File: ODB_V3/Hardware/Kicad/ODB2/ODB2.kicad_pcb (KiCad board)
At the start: 6 copper layers, 63.1 x 114.6 mm, 237 parts, among them IC1 W25Q512JVEIQ, J1 Screw_Terminal_01x08, J10 GPS_Conn_02x04_Top_Bottom, J11 Conn_02x04_Odd_Even, J15 Vin_XT30PW-F, J2 RFD_GT17HN-4DP-2HA56, J3 SYS_SW_Conn_01x05_Header, J5 MEM2067, J6 IdeFIX_GT17HN-4DP-2HA56, U1 STM32F412ZGTx, U10 ADXL382-2BCCZ-RL7, U11 SI5442DU-T1-GE3, U12 SI5442DU-T1-GE3, U13 L6981N33DR, U2 LM339, U3 SI5442DU-T1-GE3, U4 MS580301BA01-00, U6 BNO055, U7 MPQ9843GLE-5-AEC1-Z, U8 SI5442DU-T1-GE3, U9 MAX6612MXK, Y1 ABM8G-25.000MHZ-18-D2Y-T

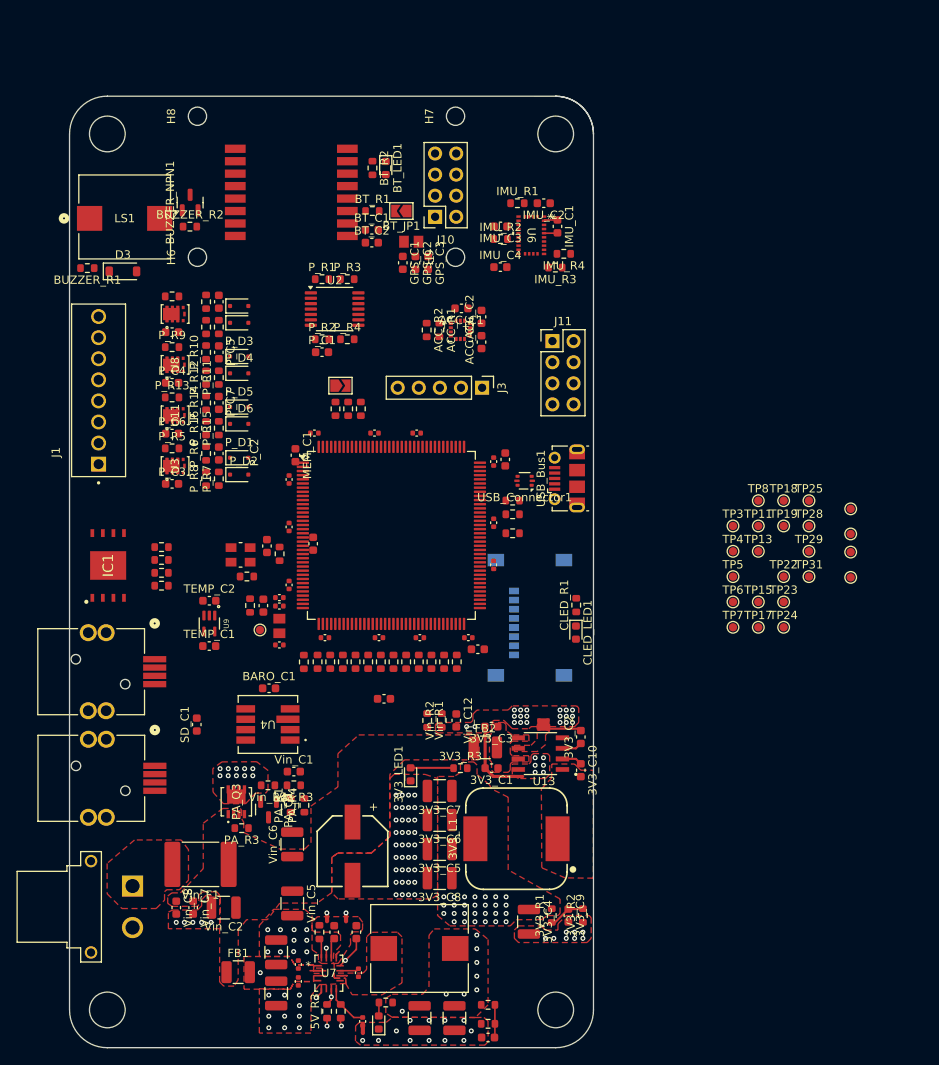
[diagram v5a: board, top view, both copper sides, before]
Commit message: fix: disconnected edge
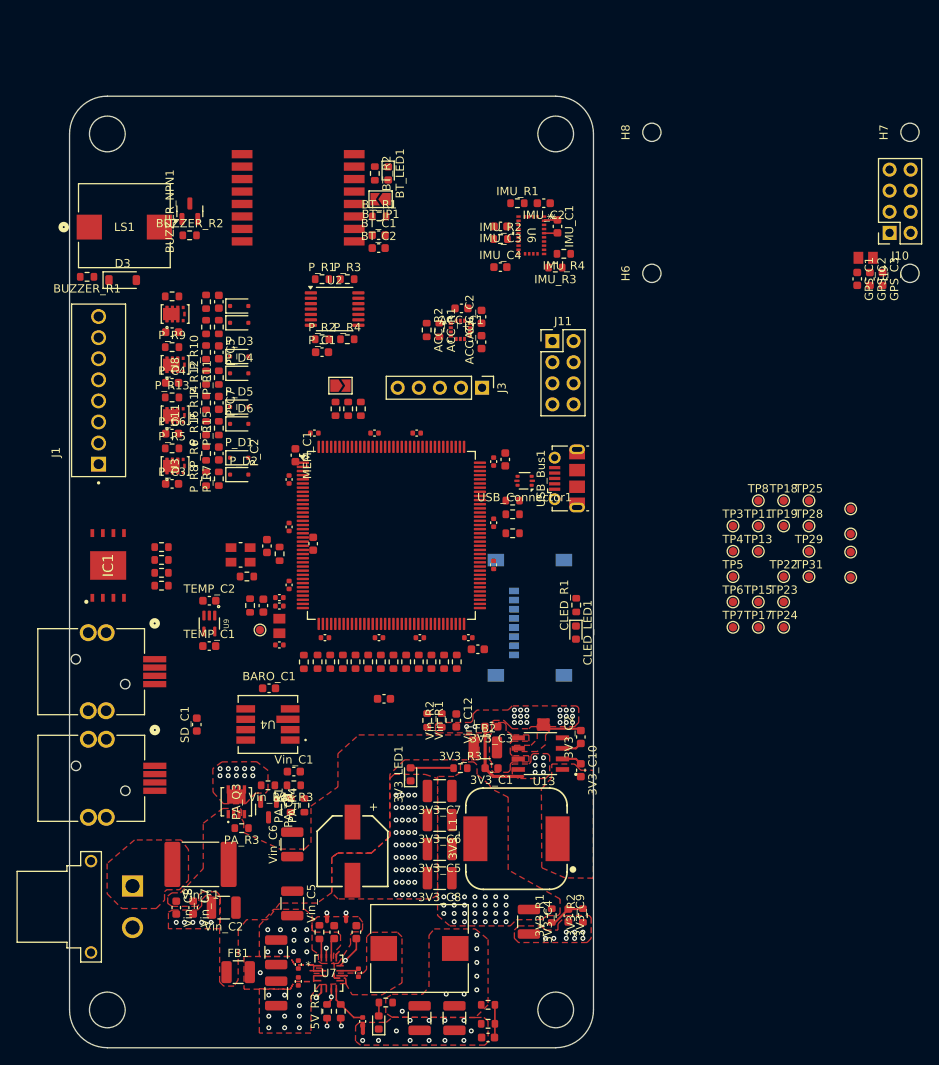
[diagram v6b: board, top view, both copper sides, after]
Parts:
- moved GPS_C1 54.8 mm to (212.3, 63.5)
- moved GPS_FB1 54.8 mm to (213.3, 60.9)
- moved J10 54.8 mm to (216.2, 57.9)
- moved GPS_C2 54.8 mm to (213.8, 63.5)
- moved GPS_C3 54.8 mm to (215.4, 63.5)
- moved H6 54.8 mm to (187.6, 62.8)
- moved H7 54.8 mm to (218.7, 45.8)
- moved H8 54.8 mm to (187.6, 45.8)
- moved H9 54.8 mm to (218.7, 62.8)
- moved BT_JP1 2.87 mm to (154.9, 53.9)
- moved BUZZER_R2 1.05 mm to (131.9, 58.2)
- moved BUZZER_NPN1 1.05 mm to (131.9, 55.3)
- moved BUZZER_R1 1.05 mm to (119.6, 63.2)
- moved D3 1.05 mm to (123.8, 63.6)
- moved LS1 1.05 mm to (124.1, 57.0)
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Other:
- outline, holes or cut-outs redrawn
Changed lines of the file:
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@@
 	(footprint "MountingHole:MountingHole_2.2mm_M2"
 		(layer "F.Cu")
-		(at 132.853519 43.866974 90)
+		(at 187.5846 45.8018 90)
 		(descr "Mounting Hole 2.2mm, M2, no annular, generated by kicad-footprint-generator mountinghole.py")
 		(tags "mountinghole M2")
@@
 	(footprint "ODB:SMTB-0927-TW-R_PUI"
 		(layer "F.Cu")
-		(at 124.087349 55.998685)
+		(at 124.0536 57.0484)
 		(tags "SMTB-0927-TW-R ")
 		(property "Reference" "LS1"
@@
 	(footprint "Capacitor_SMD:C_0603_1608Metric"
 		(layer "F.Cu")
-		(at 160.632273 61.534809 -90)
+		(at 215.363354 63.469635 -90)
 		(descr "Capacitor SMD 0603 (1608 Metric), square (rectangular) end terminal, IPC-7351 nominal, (Body size source: IPC-SM-782 page 76, https://www.pcb-3d.com/wordpress/wp-content/uploads/ipc-sm-782a_amendment_1_and_2.pdf), generated with kicad-footprint-generator")
 		(tags "capacitor")
@@
 	(footprint "MountingHole:MountingHole_2.2mm_M2"
 		(layer "F.Cu")
-		(at 163.937519 43.866974 90)
+		(at 218.6686 45.8018 90)
 		(descr "Mounting Hole 2.2mm, M2, no annular, generated by kicad-footprint-generator mountinghole.py")
 		(tags "mountinghole M2")
@@
 	(footprint "MountingHole:MountingHole_2.2mm_M2"
 		(layer "F.Cu")
-		(at 132.853519 60.853974 90)
+		(at 187.5846 62.7888 90)
 		(descr "Mounting Hole 2.2mm, M2, no annular, generated by kicad-footprint-generator mountinghole.py")
 		(tags "mountinghole M2")
@@
 	(footprint "Resistor_SMD:R_0603_1608Metric"
 		(layer "F.Cu")
-		(at 153.92012 55.285515)
+		(at 154.7436 55.9364)
 		(descr "Resistor SMD 0603 (1608 Metric), square (rectangular) end terminal, IPC-7351 nominal, (Body size source: IPC-SM-782 page 72, https://www.pcb-3d.com/wordpress/wp-content/uploads/ipc-sm-782a_amendment_1_and_2.pdf), generated with kicad-footprint-generator")
 		(tags "resistor")
@@
 	(footprint "Capacitor_SMD:C_0603_1608Metric"
 		(layer "F.Cu")
-		(at 153.85612 57.546115)
+		(at 154.6796 58.197)
 		(descr "Capacitor SMD 0603 (1608 Metric), square (rectangular) end terminal, IPC-7351 nominal, (Body size source: IPC-SM-782 page 76, https://www.pcb-3d.com/wordpress/wp-content/uploads/ipc-sm-782a_amendment_1_and_2.pdf), generated with kicad-footprint-generator")
 		(tags "capacitor")
@@
 	(footprint "Diode_SMD:D_SOD-123"
 		(layer "F.Cu")
-		(at 123.877399 62.552947)
+		(at 123.84365 63.602662)
 		(descr "SOD-123")
 		(tags "SOD-123")
@@
 	(footprint "Resistor_SMD:R_0603_1608Metric"
 		(layer "F.Cu")
-		(at 131.946607 57.161531)
+		(at 131.912858 58.211246)
 		(descr "Resistor SMD 0603 (1608 Metric), square (rectangular) end terminal, IPC-7351 nominal, (Body size source: IPC-SM-782 page 72, https://www.pcb-3d.com/wordpress/wp-content/uploads/ipc-sm-782a_amendment_1_and_2.pdf), generated with kicad-footprint-generator")
 		(tags "resistor")
@@
 	(footprint "Capacitor_SMD:C_0603_1608Metric"
 		(layer "F.Cu")
-		(at 159.108273 61.534809 -90)
+		(at 213.839354 63.469635 -90)
 		(descr "Capacitor SMD 0603 (1608 Metric), square (rectangular) end terminal, IPC-7351 nominal, (Body size source: IPC-SM-782 page 76, https://www.pcb-3d.com/wordpress/wp-content/uploads/ipc-sm-782a_amendment_1_and_2.pdf), generated with kicad-footprint-generator")
 		(tags "capacitor")
@@
 	(footprint "Capacitor_SMD:C_0603_1608Metric"
 		(layer "F.Cu")
-		(at 153.85612 59.095515)
+		(at 154.6796 59.7464)
 		(descr "Capacitor SMD 0603 (1608 Metric), square (rectangular) end terminal, IPC-7351 nominal, (Body size source: IPC-SM-782 page 76, https://www.pcb-3d.com/wordpress/wp-content/uploads/ipc-sm-782a_amendment_1_and_2.pdf), generated with kicad-footprint-generator")
 		(tags "capacitor")
@@
 	(footprint "Resistor_SMD:R_0603_1608Metric"
 		(layer "F.Cu")
-		(at 153.93232 50.103915 -90)
+		(at 154.21408 50.7548 -90)
 		(descr "Resistor SMD 0603 (1608 Metric), square (rectangular) end terminal, IPC-7351 nominal, (Body size source: IPC-SM-782 page 72, https://www.pcb-3d.com/wordpress/wp-content/uploads/ipc-sm-782a_amendment_1_and_2.pdf), generated with kicad-footprint-generator")
 		(tags "resistor")
@@
 	(footprint "Capacitor_SMD:C_0603_1608Metric"
 		(layer "F.Cu")
-		(at 157.584273 61.521809 -90)
+		(at 212.315354 63.456635 -90)
 		(descr "Capacitor SMD 0603 (1608 Metric), square (rectangular) end terminal, IPC-7351 nominal, (Body size source: IPC-SM-782 page 76, https://www.pcb-3d.com/wordpress/wp-content/uploads/ipc-sm-782a_amendment_1_and_2.pdf), generated with kicad-footprint-generator")
 		(tags "capacitor")
@@
 	(footprint "ODB:IND_25_0805_FRT"
 		(layer "F.Cu")
-		(at 158.600273 58.981809)
+		(at 213.331354 60.916635)
 		(tags "2508051217Y6 ")
 		(property "Reference" "GPS_FB1"
@@
 			(polygon
 				(pts
-					(xy 158.358973 58.308709) (xy 158.841573 58.308709) (xy 158.841573 59.654909) (xy 158.358973 59.654909)
+					(xy 213.090054 60.243535) (xy 213.572654 60.243535) (xy 213.572654 61.589735) (xy 213.090054 61.589735)
 				)
 			)
@@
 	(footprint "MountingHole:MountingHole_2.2mm_M2"
 		(layer "F.Cu")
-		(at 163.937519 60.853974 90)
+		(at 218.6686 62.7888 90)
 		(descr "Mounting Hole 2.2mm, M2, no annular, generated by kicad-footprint-generator mountinghole.py")
 		(tags "mountinghole M2")
@@
 	(footprint "Connector_PinSocket_2.54mm:PinSocket_2x04_P2.54mm_Vertical"
 		(layer "F.Cu")
-		(at 161.476519 55.979974 180)
+		(at 216.2076 57.9148 180)
 		(descr "Through hole straight socket strip, 2x04, 2.54mm pitch, double cols (from Kicad 4.0.7), script generated")
 		(tags "Through hole socket strip THT 2x04 2.54mm double row")
@@
 	(footprint "Resistor_SMD:R_0603_1608Metric"
 		(layer "F.Cu")
-		(at 119.595001 62.158516 180)
+		(at 119.561252 63.208231 180)
 		(descr "Resistor SMD 0603 (1608 Metric), square (rectangular) end terminal, IPC-7351 nominal, (Body size source: IPC-SM-782 page 72, https://www.pcb-3d.com/wordpress/wp-content/uploads/ipc-sm-782a_amendment_1_and_2.pdf), generated with kicad-footprint-generator")
 		(tags "resistor")
@@
 	(footprint "LED_SMD:LED_0603_1608Metric"
 		(layer "F.Cu")
-		(at 155.53252 50.103915 -90)
+		(at 155.8226 50.759 -90)
 		(descr "LED SMD 0603 (1608 Metric), square (rectangular) end terminal, IPC-7351 nominal, (Body size source: http://www.tortai-tech.com/upload/download/2011102023233369053.pdf), generated with kicad-footprint-generator")
 		(tags "LED")
@@
 	(footprint "ODB:hm11"
 		(layer "F.Cu")
-		(at 143.90972 50.786915)
+		(at 144.7332 51.4378)
 		(property "Reference" "H5"
 			(at 0 -0.5 0)
@@
 	(footprint "Jumper:SolderJumper-2_P1.3mm_Open_TrianglePad1.0x1.5mm"
 		(layer "F.Cu")
-		(at 157.41212 55.285515 180)
+		(at 154.91368 53.863885 180)
 		(descr "SMD Solder Jumper, 1x1.5mm Triangular Pads, 0.3mm gap, open")
 		(tags "solder jumper open")
@@
 	(footprint "Package_TO_SOT_SMD:SOT-23"
 		(layer "F.Cu")
-		(at 131.972007 54.265931 90)
+		(at 131.938258 55.315646 90)
 		(descr "SOT, 3 Pin (JEDEC TO-236 Var AB https://www.jedec.org/document_search?search_api_views_fulltext=TO-236), generated with kicad-footprint-generator ipc_gullwing_generator.py")
 		(tags "SOT TO_SOT_SMD")
@@
 	)
 	(gr_line
-		(start 122 156.05)
-		(end 176 156.05)
+		(start 121.9962 156.0576)
+		(end 176 156.0576)
 		(stroke
 			(width 0.05)
@@
 	)
 	(gr_line
-		(start 180.55 46.015094)
-		(end 180.55 151.5)
-		(stroke
-			(width 0.05)
-			(type default)
-		)
-		(layer "Edge.Cuts")
-	)
-	(gr_arc
-		(start 176.001256 41.459605)
-		(mid 179.217704 42.791901)
-		(end 180.55 46.008349)
+		(start 180.549991 46)
+		(end 180.549991 151.5)
 		(stroke
 			(width 0.05)
@@
 	)
 	(gr_line
-		(start 122 41.45)
-		(end 176 41.459606)
+		(start 122 41.4528)
+		(end 176 41.4528)
 		(stroke
 			(width 0.05)
@@
 	)
 	(gr_line
-		(start 117.45 46)
-		(end 117.45 151.5)
+		(start 117.4496 45.9994)
+		(end 117.4496 151.5)
 		(stroke
 			(width 0.05)

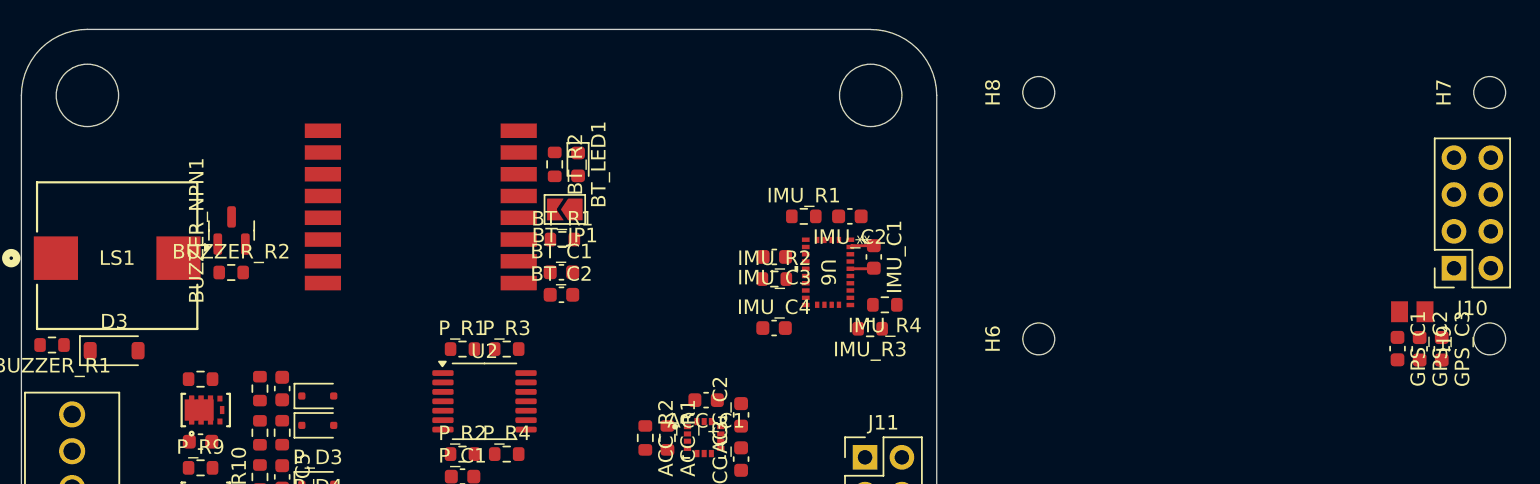
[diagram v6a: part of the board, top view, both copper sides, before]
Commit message: wip: add rounded edge to hm11
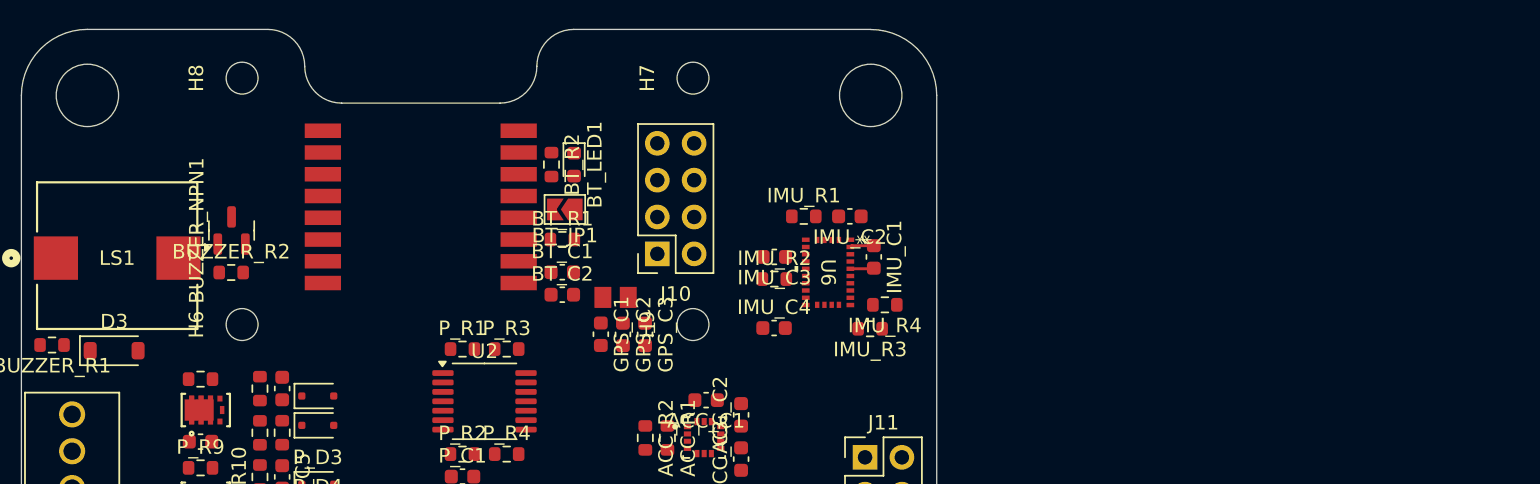
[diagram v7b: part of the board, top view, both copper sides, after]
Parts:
- moved GPS_C1 54.9 mm to (157.4, 62.5)
- moved GPS_C3 54.9 mm to (160.4, 62.5)
- moved GPS_FB1 54.9 mm to (158.4, 59.9)
- moved H6 54.9 mm to (132.7, 61.8)
- moved H7 54.9 mm to (163.7, 44.8)
- moved H8 54.9 mm to (132.7, 44.8)
- moved H9 54.9 mm to (163.7, 61.8)
- moved J10 54.9 mm to (161.3, 56.9)
- moved GPS_C2 54.9 mm to (158.9, 62.5)
- moved BT_LED1 0.27 mm to (155.5, 50.8)
- moved BT_R2 0.22 mm to (154.0, 50.8)
- moved BT_C1 0.06 mm to (154.7, 58.2)
- moved BT_C2 0.06 mm to (154.7, 59.7)
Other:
- outline, holes or cut-outs redrawn
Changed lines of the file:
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@@
 	(footprint "MountingHole:MountingHole_2.2mm_M2"
 		(layer "F.Cu")
-		(at 187.5846 45.8018 90)
+		(at 132.6642 44.8112 90)
 		(descr "Mounting Hole 2.2mm, M2, no annular, generated by kicad-footprint-generator mountinghole.py")
 		(tags "mountinghole M2")
@@
 	(footprint "Capacitor_SMD:C_0603_1608Metric"
 		(layer "F.Cu")
-		(at 215.363354 63.469635 -90)
+		(at 160.442954 62.479035 -90)
 		(descr "Capacitor SMD 0603 (1608 Metric), square (rectangular) end terminal, IPC-7351 nominal, (Body size source: IPC-SM-782 page 76, https://www.pcb-3d.com/wordpress/wp-content/uploads/ipc-sm-782a_amendment_1_and_2.pdf), generated with kicad-footprint-generator")
 		(tags "capacitor")
@@
 	(footprint "MountingHole:MountingHole_2.2mm_M2"
 		(layer "F.Cu")
-		(at 218.6686 45.8018 90)
+		(at 163.7482 44.8112 90)
 		(descr "Mounting Hole 2.2mm, M2, no annular, generated by kicad-footprint-generator mountinghole.py")
 		(tags "mountinghole M2")
@@
 	(footprint "MountingHole:MountingHole_2.2mm_M2"
 		(layer "F.Cu")
-		(at 187.5846 62.7888 90)
+		(at 132.6642 61.7982 90)
 		(descr "Mounting Hole 2.2mm, M2, no annular, generated by kicad-footprint-generator mountinghole.py")
 		(tags "mountinghole M2")
@@
 	(footprint "Capacitor_SMD:C_0603_1608Metric"
 		(layer "F.Cu")
-		(at 154.6796 58.197)
+		(at 154.7368 58.1914)
 		(descr "Capacitor SMD 0603 (1608 Metric), square (rectangular) end terminal, IPC-7351 nominal, (Body size source: IPC-SM-782 page 76, https://www.pcb-3d.com/wordpress/wp-content/uploads/ipc-sm-782a_amendment_1_and_2.pdf), generated with kicad-footprint-generator")
 		(tags "capacitor")
@@
 	(footprint "Capacitor_SMD:C_0603_1608Metric"
 		(layer "F.Cu")
-		(at 213.839354 63.469635 -90)
+		(at 158.918954 62.479035 -90)
 		(descr "Capacitor SMD 0603 (1608 Metric), square (rectangular) end terminal, IPC-7351 nominal, (Body size source: IPC-SM-782 page 76, https://www.pcb-3d.com/wordpress/wp-content/uploads/ipc-sm-782a_amendment_1_and_2.pdf), generated with kicad-footprint-generator")
 		(tags "capacitor")
@@
 	(footprint "Capacitor_SMD:C_0603_1608Metric"
 		(layer "F.Cu")
-		(at 154.6796 59.7464)
+		(at 154.7368 59.7408)
 		(descr "Capacitor SMD 0603 (1608 Metric), square (rectangular) end terminal, IPC-7351 nominal, (Body size source: IPC-SM-782 page 76, https://www.pcb-3d.com/wordpress/wp-content/uploads/ipc-sm-782a_amendment_1_and_2.pdf), generated with kicad-footprint-generator")
 		(tags "capacitor")
@@
 	(footprint "Resistor_SMD:R_0603_1608Metric"
 		(layer "F.Cu")
-		(at 154.21408 50.7548 -90)
+		(at 153.99188 50.7704 -90)
 		(descr "Resistor SMD 0603 (1608 Metric), square (rectangular) end terminal, IPC-7351 nominal, (Body size source: IPC-SM-782 page 72, https://www.pcb-3d.com/wordpress/wp-content/uploads/ipc-sm-782a_amendment_1_and_2.pdf), generated with kicad-footprint-generator")
 		(tags "resistor")
@@
 	(footprint "Capacitor_SMD:C_0603_1608Metric"
 		(layer "F.Cu")
-		(at 212.315354 63.456635 -90)
+		(at 157.394954 62.466035 -90)
 		(descr "Capacitor SMD 0603 (1608 Metric), square (rectangular) end terminal, IPC-7351 nominal, (Body size source: IPC-SM-782 page 76, https://www.pcb-3d.com/wordpress/wp-content/uploads/ipc-sm-782a_amendment_1_and_2.pdf), generated with kicad-footprint-generator")
 		(tags "capacitor")
@@
 	(footprint "ODB:IND_25_0805_FRT"
 		(layer "F.Cu")
-		(at 213.331354 60.916635)
+		(at 158.410954 59.926035)
 		(tags "2508051217Y6 ")
 		(property "Reference" "GPS_FB1"
@@
 			(polygon
 				(pts
-					(xy 213.090054 60.243535) (xy 213.572654 60.243535) (xy 213.572654 61.589735) (xy 213.090054 61.589735)
+					(xy 158.169654 59.252935) (xy 158.652254 59.252935) (xy 158.652254 60.599135) (xy 158.169654 60.599135)
 				)
 			)
@@
 	(footprint "MountingHole:MountingHole_2.2mm_M2"
 		(layer "F.Cu")
-		(at 218.6686 62.7888 90)
+		(at 163.7482 61.7982 90)
 		(descr "Mounting Hole 2.2mm, M2, no annular, generated by kicad-footprint-generator mountinghole.py")
 		(tags "mountinghole M2")
@@
 	(footprint "Connector_PinSocket_2.54mm:PinSocket_2x04_P2.54mm_Vertical"
 		(layer "F.Cu")
-		(at 216.2076 57.9148 180)
+		(at 161.2872 56.9242 180)
 		(descr "Through hole straight socket strip, 2x04, 2.54mm pitch, double cols (from Kicad 4.0.7), script generated")
 		(tags "Through hole socket strip THT 2x04 2.54mm double row")
@@
 	(footprint "LED_SMD:LED_0603_1608Metric"
 		(layer "F.Cu")
-		(at 155.8226 50.759 -90)
+		(at 155.5496 50.7746 -90)
 		(descr "LED SMD 0603 (1608 Metric), square (rectangular) end terminal, IPC-7351 nominal, (Body size source: http://www.tortai-tech.com/upload/download/2011102023233369053.pdf), generated with kicad-footprint-generator")
 		(tags "LED")
@@
 		(embedded_fonts no)
 	)
+	(gr_line
+		(start 176 41.4528)
+		(end 155.524595 41.4528)
+		(stroke
+			(width 0.05)
+			(type default)
+		)
+		(layer "Edge.Cuts")
+	)
+	(gr_arc
+		(start 152.984595 43.9928)
+		(mid 153.728544 42.196749)
+		(end 155.524595 41.4528)
+		(stroke
+			(width 0.05)
+			(type default)
+		)
+		(layer "Edge.Cuts")
+	)
 	(gr_arc
 		(start 122 156.05)
@@
 		(layer "Edge.Cuts")
 	)
+	(gr_arc
+		(start 152.984595 43.9928)
+		(mid 152.240646 45.788851)
+		(end 150.444595 46.5328)
+		(stroke
+			(width 0.05)
+			(type default)
+		)
+		(layer "Edge.Cuts")
+	)
+	(gr_line
+		(start 139.5222 46.5328)
+		(end 150.4442 46.5328)
+		(stroke
+			(width 0.05)
+			(type default)
+		)
+		(layer "Edge.Cuts")
+	)
+	(gr_arc
+		(start 139.5222 46.5328)
+		(mid 137.726149 45.788851)
+		(end 136.9822 43.9928)
+		(stroke
+			(width 0.05)
+			(type default)
+		)
+		(layer "Edge.Cuts")
+	)
 	(gr_line
 		(start 121.9962 156.0576)
@@
 	)
 	(gr_arc
+		(start 134.4422 41.4528)
+		(mid 136.238251 42.196749)
+		(end 136.9822 43.9928)
+		(stroke
+			(width 0.05)
+			(type default)
+		)
+		(layer "Edge.Cuts")
+	)
+	(gr_arc
 		(start 117.45 46)
 		(mid 118.782664 42.782664)
@@
 	(gr_line
 		(start 122 41.4528)
-		(end 176 41.4528)
+		(end 134.4422 41.4528)
 		(stroke
 			(width 0.05)
